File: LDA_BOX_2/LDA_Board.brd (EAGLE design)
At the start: 78 x 55 mm, 77 parts, among them IC1 STM32F407ZET, SW3P-1 LD-CCB-001, SW3P-2 LD-CCB-001, Y1 8MHZ

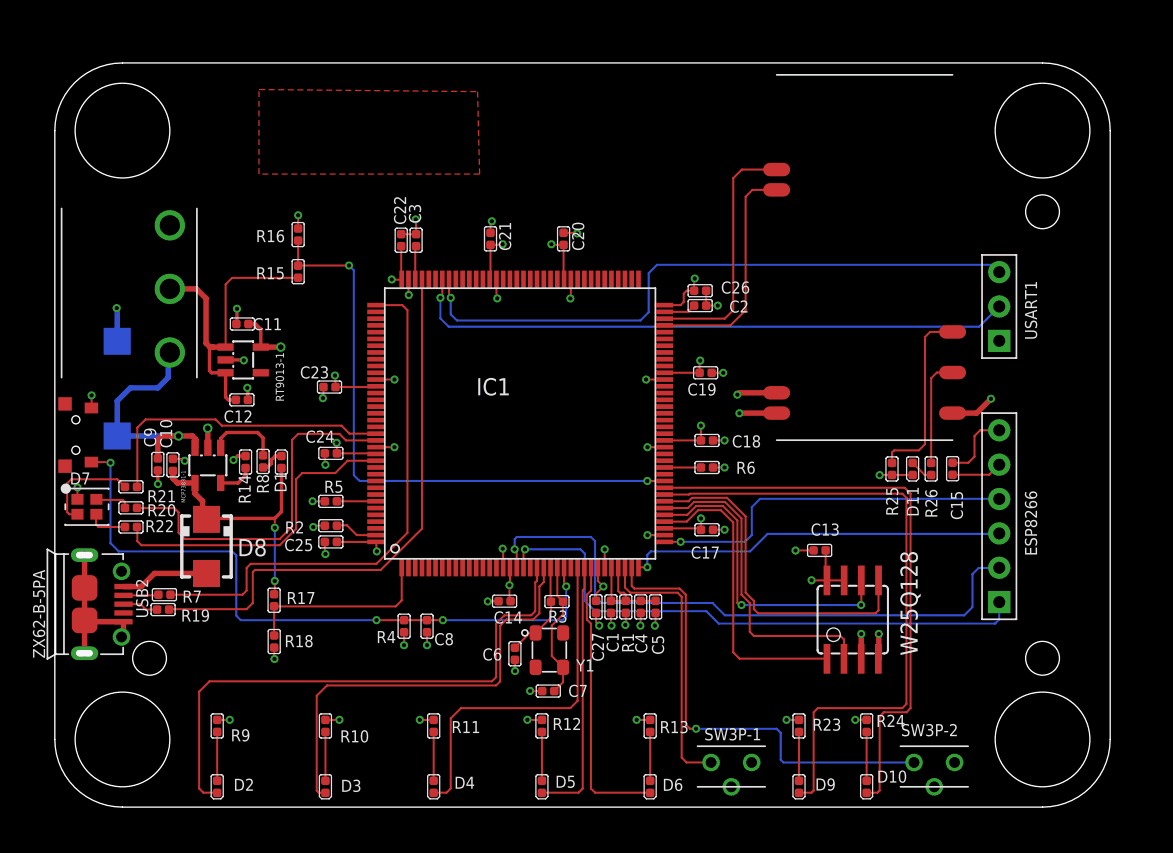
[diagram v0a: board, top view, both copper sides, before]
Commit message: 第二版盒子，器件在一端
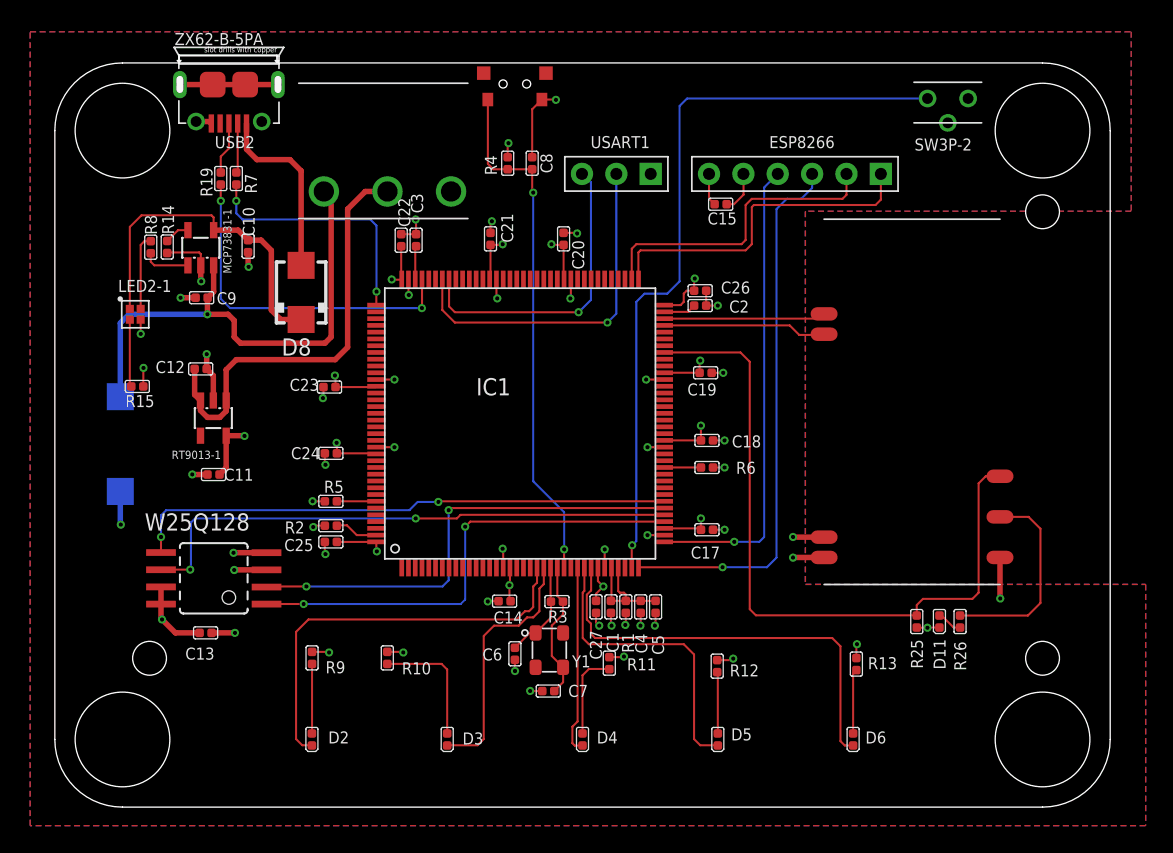
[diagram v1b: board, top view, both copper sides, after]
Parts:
- removed D1, D10, D9: BLUE-0402, 1-LDA_Board:LED-0402
- removed D7: HSMF-C118, 1-LDA_Board:LED4-SMD-1210
- removed R16, R17: 10k, 1-LDA_Board:R0402
- removed R18: 20k, 1-LDA_Board:R0402
- removed R20, R21, R22, R23, R24: 510R, 1-LDA_Board:R0402
- removed SW3P-1: LD-CCB-001, 1-LDA_Board:SW3-2.54-9.0X3.5X3.5+2.0MM
- added LED2-1: DOUBLE_LED, 1-LDA_Board:LED2-SMD-1010
- R15: value 10k -> 470R
- moved SW3P-2 49.1 mm to (66.0, 50.6)
- moved W25Q128 47.3 mm to (11.7, 16.9), turned to 90 degrees
- moved C13 45.8 mm to (11.1, 12.9), turned to 270 degrees
- moved B-1 41.5 mm to (34.0, 53.4), turned to 180 degrees
- moved USB2 39.9 mm to (12.9, 53.4), turned to 180 degrees
- moved C8 35.1 mm to (35.3, 47.6), turned to 0 degrees
- moved R4 35.1 mm to (33.5, 47.6), turned to 180 degrees
- moved R19 32.1 mm to (12.3, 46.5), turned to 0 degrees
- moved R7 31.2 mm to (13.4, 46.5), turned to 0 degrees
- moved USART1 29.9 mm to (41.5, 46.8), turned to 270 degrees
- moved ESP8266 29.5 mm to (54.7, 46.8), turned to 270 degrees
- moved C15 26.0 mm to (49.2, 44.6), turned to 90 degrees
- moved D8 20.0 mm to (18.2, 38.0), turned to 90 degrees
- moved R8 17.9 mm to (7.09, 41.4), turned to 0 degrees
- moved SW-1 17.6 mm to (24.6, 45.5), turned to 180 degrees
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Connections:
- removed net LED6: D9.-, IC1.44
- removed net LED7: D10.-, IC1.45
- removed net LED_B: IC1.129, R20.1
- removed net LED_G: IC1.132, R22.1
- removed net LED_R: IC1.128, R21.1
- removed net LI_CHARGE: IC1.1, R17.2, R18.1
- removed net LI_QUANTITY: IC1.46, R15.2, R16.1
- removed net N$10: D7.4, R20.2
- removed net N$12: D7.2, R21.2
- removed net N$18: D7.3, R22.2
- removed net N$24: D9.+, R23.2
- removed net N$25: D10.+, R24.2
- removed net WK_UP: IC1.34, SW3P-1.2
- new net BT_RESET: HC05-1.P$26, IC1.65, R25.1
- net +3.7V: no longer R15.1
- net +3V3: now also R15.1; no longer R23.1, R24.1, SW3P-1.1
- net +5V: now also LED2-1.1; no longer D1.+, R17.1
- net GBC_KEY: now also IC1.74; no longer IC1.18
- net GBC_LED: now also IC1.73; no longer IC1.19
- net GND: now also LED2-1.3; no longer D7.1, R16.2, R18.2
- net N$16: now also LED2-1.4; no longer D1.-
- net N$17: now also LED2-1.2, R15.2; no longer HC05-1.P$26, R25.1
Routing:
- net BT_RESET: track 0.00 -> 53.1 mm
- net LED6: track 47.4 -> 0.00 mm
- net LI_QUANTITY: track 44.4 -> 0.00 mm, vias 2 -> 0
- net LED7: track 43.3 -> 0.00 mm
- net LED_B: track 26.7 -> 0.00 mm
- net TX1: track 47.0 -> 22.6 mm
- net LED_G: track 23.6 -> 0.00 mm
- net GBC_KEY: track 45.7 -> 22.9 mm, vias 1 -> 0
- net LED_R: track 22.7 -> 0.00 mm
- net KEY1: track 34.4 -> 55.1 mm
- net CLK: track 39.3 -> 18.7 mm, vias 0 -> 2
- net WK_UP: track 20.2 -> 0.00 mm
- net BATTERY: track 18.6 -> 37.9 mm
- net RX1: track 45.1 -> 26.1 mm
- net SPI1_CLK: track 23.6 -> 40.9 mm
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- added copper zone on layer 1, net N$10
- added copper zone on layer 16, net N$12
- removed copper zone on layer 1, net N$21
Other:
- board text added: "Econ-Tech"
- board text removed: "ECON-TECH"
